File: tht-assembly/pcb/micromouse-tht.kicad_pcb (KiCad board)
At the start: 2 copper layers, 100 x 120 mm, 161 parts, among them J1 JST_XH_B2B-XH-A_1x02_P2.50mm_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, J10 AMASS_XT60-M_1x02_P7.20mm_Ver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, J11 PinSocket_1x08_P2.54mm_Vertic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, J12 PinSocket_1x08_P2.54mm_Vertic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, J13 PinSocket_1x22_P2.54mm_Vertic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, J14 PinSocket_1x22_P2.54mm_Vertic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, J15 PinSocket_1x06_P2.54mm_Vertic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, J5 JST_ZH_B6B-ZR_1x06_P1.50mm_Ve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, J6 JST_ZH_B6B-ZR_1x06_P1.50mm_Ve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, J8 PinHeader_1x06_P2.54mm_Vertic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, J9 JST_XH_B3B-XH-A_1x03_P2.50mm_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, Q1 TO-220-3_Vertical, Q121 TO-92_Inline, Q122 TO-92_Inline, Q123 TO-92_Inline, Q124 TO-92_Inline, Q125 TO-92_Inline, Q126 TO-92_Inline, Q131 TO-92_Inline, Q132 TO-92_Inline, Q133 TO-92_Inline, Q134 TO-92_Inline, Q135 TO-92_Inline, Q136 TO-92_Inline, Q137 TO-92_Inline, Q138 TO-92_Inline, Q16 TO-92_Inline, Q17 TO-92_Inline, Q18 TO-92_Inline, Q19 TO-92_Inline, Q2 LED_D5.0mm_IRBlack, Q3 LED_D5.0mm_IRBlack, Q34 TO-92_Inline, Q35 TO-92_Inline, Q4 LED_D5.0mm_IRBlack, Q5 LED_D5.0mm_IRBlack, Q6 LED_D5.0mm_IRBlack, Q7 LED_D5.0mm_IRBlack, SW1 SW_PUSH_6mm, SW2 SW_PUSH_6mm, SW3 SW_PUSH_6mm, SW4 SW_PUSH_6mm, SW5 SW_Slide_SPDT_Angled_CK_OS102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, SW6 SW_Slide_SPDT_Angled_CK_OS102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, U1 TO-220-5_Vertical, U4 DIP-24_W15.24mm, U7 TO-220-5_Vertical

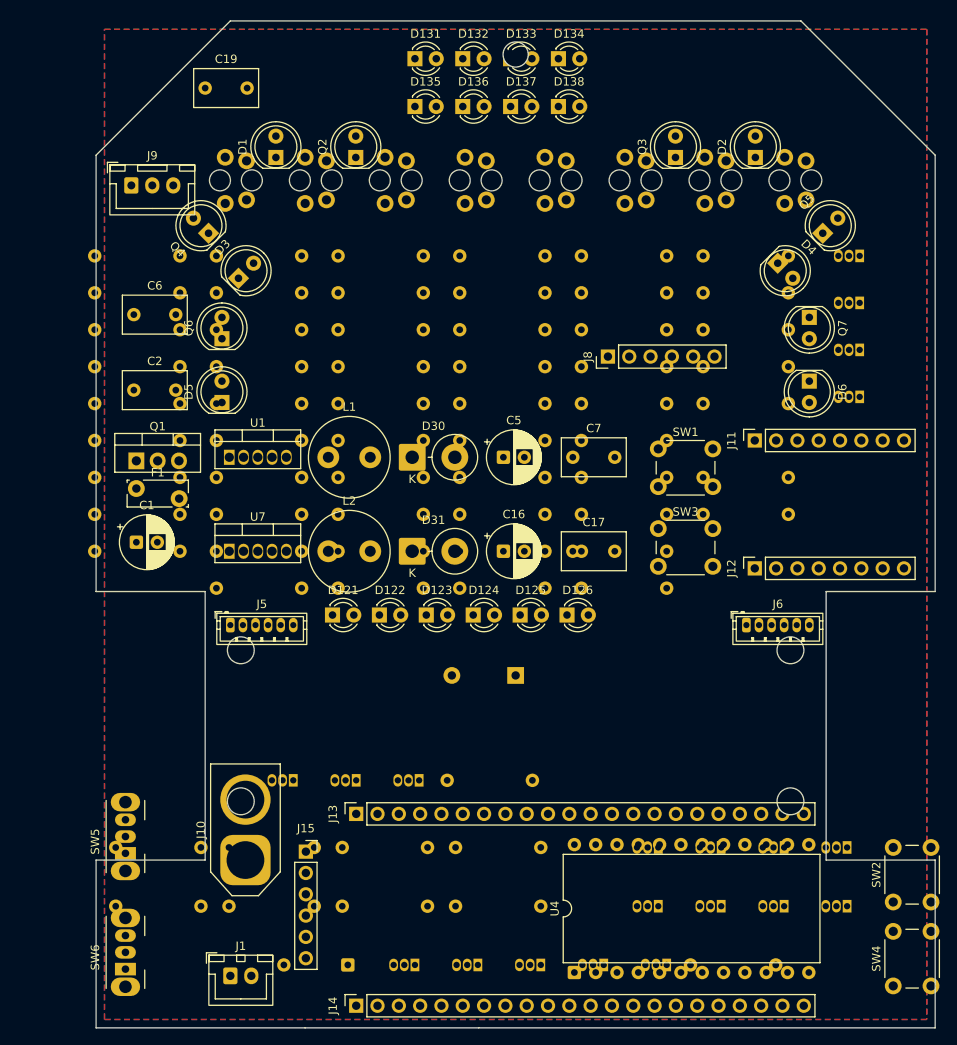
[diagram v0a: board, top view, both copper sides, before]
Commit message: THT M4 WIP: net-aware clustering placer + repair pass + visual floor-plan (11 overlaps, converging)
Replaces the routing-hostile bottom-grid placement (47% route-fail) with a
net-aware auto-placer: fixed anchors for geometry/edge parts, every support
part spiral-placed adjacent to its neighbours on the bottom face, then a
repair pass driving check_overlaps down using the accurate per-piece checker.
Down to 11 courtyard overlaps (from 83); remaining = buttons-vs-driver-socket
+ close optic pairs + mount-hole adjacencies. Router v3 (fast-fail, bounded,
incremental-save, logged) proven on the signal nets; spanning power/emitter
buses queued for hand-routing. WIP checkpoint -- not yet DRC-clean.

Co-Authored-By: Claude Fable 5 <noreply@anthropic.com>
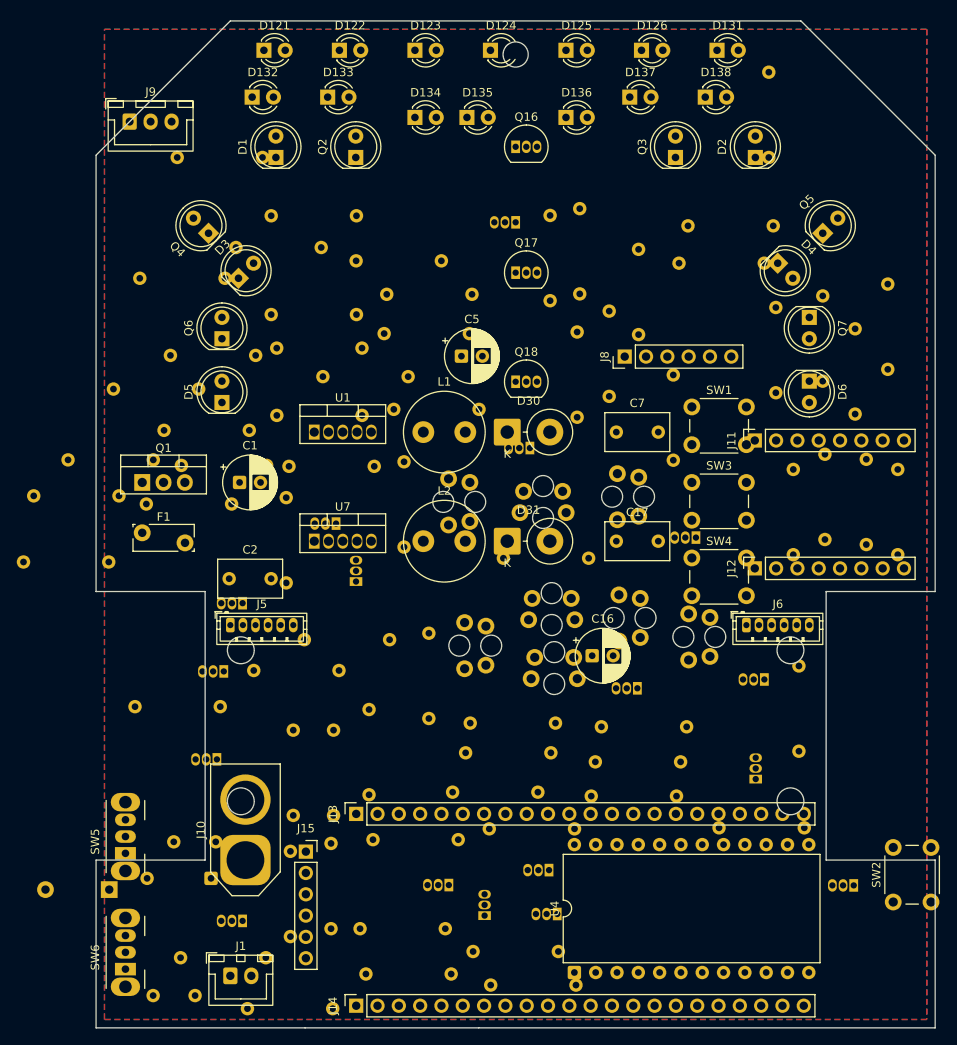
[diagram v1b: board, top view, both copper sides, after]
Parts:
- C19, C6: moved to B.Cu
- Q16, Q17, Q18: moved to F.Cu
- moved C19 108.2 mm to (11.8, 116.2), turned to 180 degrees
- moved Q16 93.8 mm to (50.0, 15.0), turned to 0 degrees
- moved R114 90.6 mm to (42.3, 113.6)
- moved R115 89.2 mm to (83.8, 87.0), turned to 90 degrees
- moved R101 84.0 mm to (86.9, 61.8), turned to 90 degrees
- moved R112 82.6 mm to (57.2, 114.9)
- moved Q17 82.0 mm to (50.0, 30.0), turned to 0 degrees
- moved R113 80.2 mm to (41.6, 108.2)
- moved R111 80.1 mm to (55.1, 110.9)
- moved R1 79.8 mm to (2.73, 56.6)
- moved R108 77.6 mm to (95.5, 63.6), turned to 90 degrees
- moved R102 75.6 mm to (91.8, 62.4), turned to 90 degrees
- moved R117 74.0 mm to (23.2, 109.1), turned to 90 degrees
- moved Q18 73.9 mm to (50.0, 43.0), turned to 0 degrees
- moved Q137 72.6 mm to (17.5, 107.2)
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
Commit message: THT placement: 5 courtyard overlaps (4 body-clear optic pairs + DevKit/bracket-hole mechanical conflict)
J6 relocated clear of the TB6612 socket; buttons to the open lower-centre;
nose LEDs dodge the castor hole. Remaining: the diagonal emitter/detector
clusters (body-clear, cosmetic) and -- the real finding -- the DevKitC-1
1x22 socket (56mm) overlaps a UKMARS motor-bracket mounting hole. The
100x120 SMD footprint cannot cleanly host a DevKit-based THT build + the
fixed bracket holes; needs a larger board or a different module mount.

Co-Authored-By: Claude Fable 5 <noreply@anthropic.com>
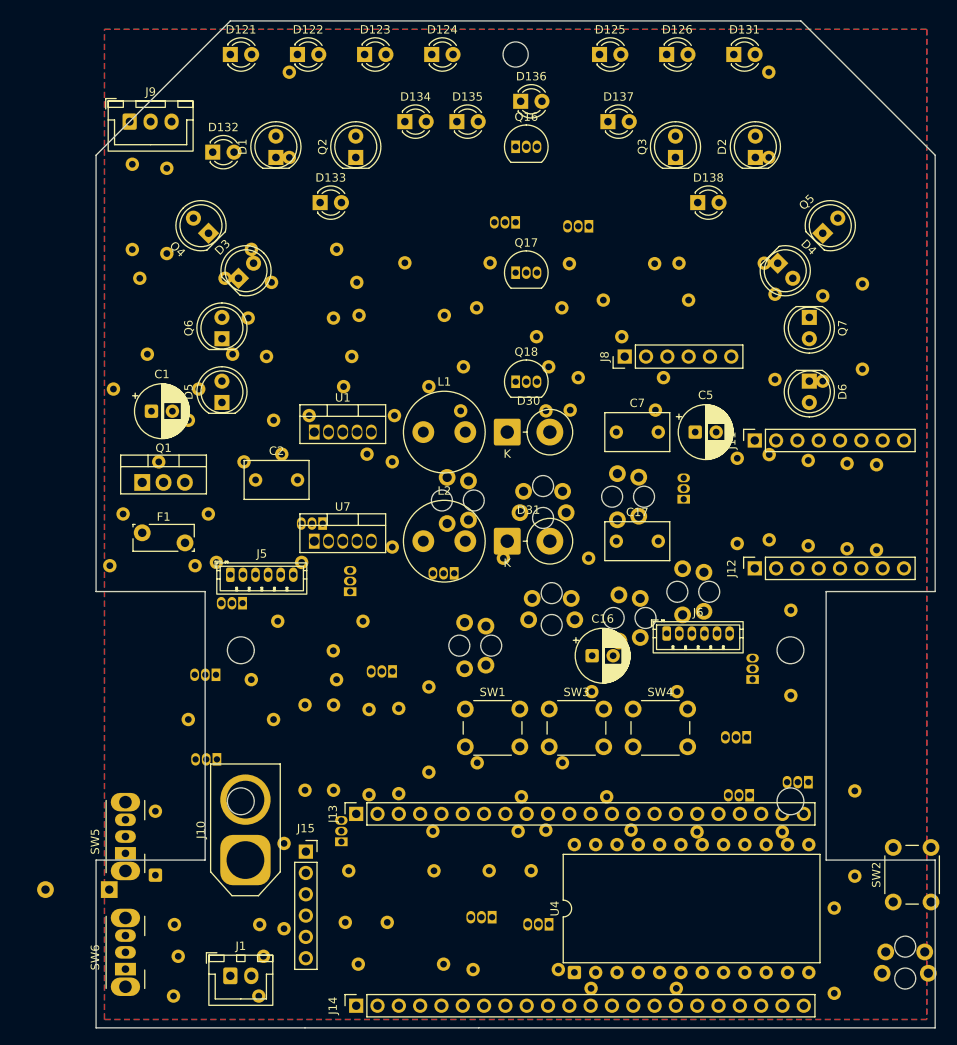
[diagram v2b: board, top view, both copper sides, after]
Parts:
- moved R107 86.9 mm to (93.0, 63.0), turned to 90 degrees
- moved R108 82.8 mm to (16.3, 39.7), turned to 180 degrees
- moved Q137 69.4 mm to (84.9, 90.7)
- moved R117 67.6 mm to (90.4, 101.9)
- moved Q138 60.4 mm to (42.7, 65.8)
- moved LS2 54.6 mm to (96.4, 112.2)
- moved R104 50.5 mm to (19.9, 111.5)
- moved R118 48.5 mm to (36.1, 92.1), turned to 90 degrees
- moved SW1 45.0 mm to (44.0, 82.0)
- moved C19 42.7 mm to (51.9, 101.3)
- moved R2 41.7 mm to (8.43, 27.7)
- moved R58 39.3 mm to (24.5, 64.5)
- moved Q124 39.2 mm to (58.7, 24.5)
- moved R105 38.1 mm to (91.3, 41.5)
- moved R142 36.4 mm to (28.7, 78.5)
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
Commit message: THT placement CLEAN: 0 courtyard overlaps (line array removed, 2 RGB LEDs added, JTAG dropped)
Per user: removed the line-follower array + mux (~50 parts -> board decongested
198->145 parts), added 2x ESP-driven common-cathode RGB LEDs (D40/D41,
Kingbright WP154A4, 6 LEDC channels via freed pins), dropped the redundant
external JTAG header (DevKit has USB-JTAG). DevKit socket recentred (x25.5) to
sit between the motor-bracket holes. Optic courtyards shrunk to body-true
circles (r=2.4) so the 45-deg diagonal emitter/detector pairs clear DRC.
verify_drc courtyard overlaps: 0. Next: route + DRC gate.

Co-Authored-By: Claude Fable 5 <noreply@anthropic.com>
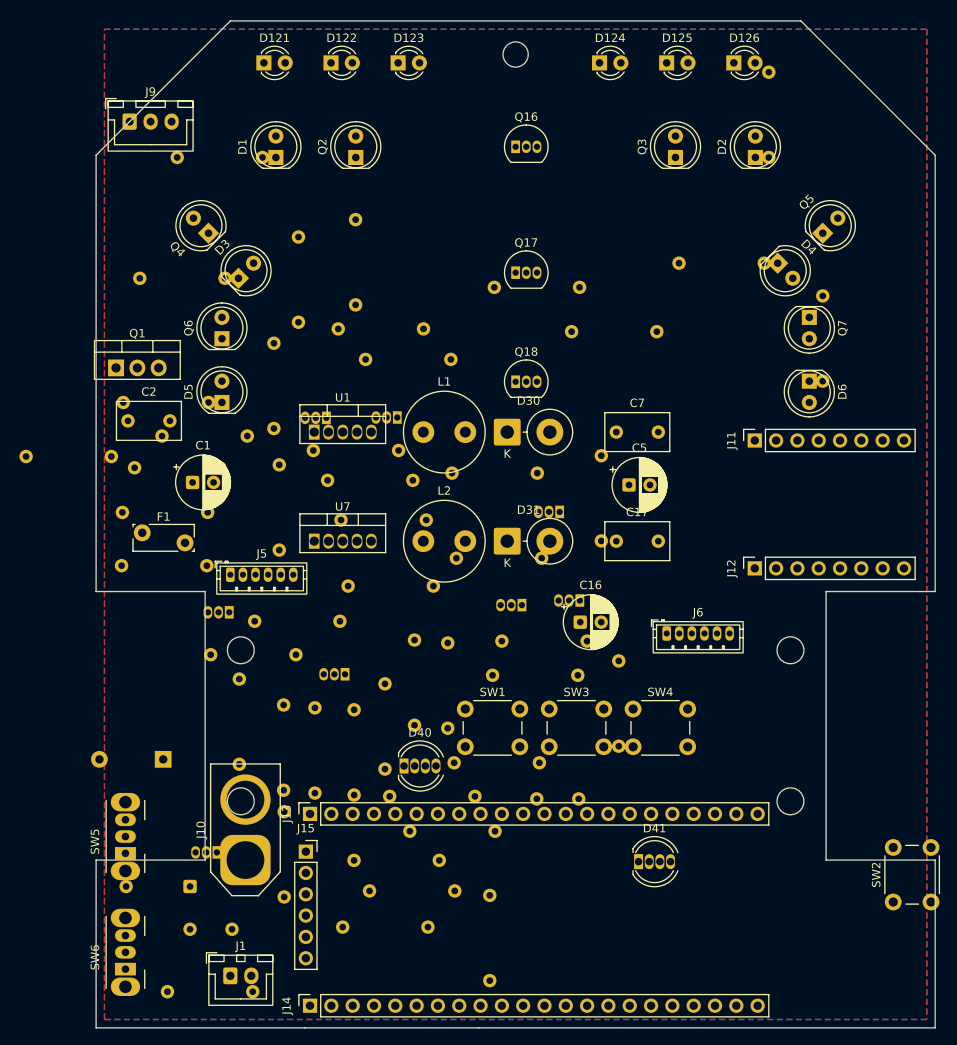
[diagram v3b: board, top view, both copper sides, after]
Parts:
- removed D131, D132, D133, D134, D135, D136, D137, D138: LED_D3.0mm, LED_D3.0mm
- removed J8: PinHeader_1x06_P2.54mm_Vertical, PinHeader_1x06_P2.54mm_Vertical
- removed LS1, LS2, LS3, LS4, LS5, LS6, LS7, LS8: TCRT5000, TCRT5000
- removed Q131, Q132, Q133, Q134, Q135, Q136, Q137, Q138, Q19: TO-92_Inline, TO-92_Inline
- removed R101, R102, R103, R104, R105, R106, R107, R108, R111, R112, R113, R114, R115, R116, R117, R118, R161, R162, R163, R164, R165, R166, R167, R168, R61: R_Axial_DIN0207_L6.3mm_D2.5mm_P10.16mm_Horizontal, R_Axial_DIN0207_L6.3mm_D2.5mm_P10.16mm_Horizontal
- removed U4: DIP-24_W15.24mm, DIP-24_W15.24mm
- added D40: LED_D5.0mm-4_RGB, LED_D5.0mm-4_RGB, F.Cu at (36.7, 88.8)
- added D41: LED_D5.0mm-4_RGB, LED_D5.0mm-4_RGB, F.Cu at (64.7, 100.2)
- added R201: R_Axial_DIN0207_L6.3mm_D2.5mm_P10.16mm_Horizontal, R_Axial_DIN0207_L6.3mm_D2.5mm_P10.16mm_Horizontal, B.Cu at (40.9, 100.0)
- added R202: R_Axial_DIN0207_L6.3mm_D2.5mm_P10.16mm_Horizontal, R_Axial_DIN0207_L6.3mm_D2.5mm_P10.16mm_Horizontal, B.Cu at (34.4, 89.2)
- added R203: R_Axial_DIN0207_L6.3mm_D2.5mm_P10.16mm_Horizontal, R_Axial_DIN0207_L6.3mm_D2.5mm_P10.16mm_Horizontal, B.Cu at (30.8, 92.2)
- added R204: R_Axial_DIN0207_L6.3mm_D2.5mm_P10.16mm_Horizontal, R_Axial_DIN0207_L6.3mm_D2.5mm_P10.16mm_Horizontal, B.Cu at (38.0, 83.9)
- added R205: R_Axial_DIN0207_L6.3mm_D2.5mm_P10.16mm_Horizontal, R_Axial_DIN0207_L6.3mm_D2.5mm_P10.16mm_Horizontal, B.Cu at (41.9, 84.3)
- added R206: R_Axial_DIN0207_L6.3mm_D2.5mm_P10.16mm_Horizontal, R_Axial_DIN0207_L6.3mm_D2.5mm_P10.16mm_Horizontal, B.Cu at (42.8, 103.7)
- moved R76 59.2 mm to (21.2, 48.6), turned to 90 degrees
- moved R9 48.7 mm to (57.4, 78.0), turned to 180 degrees
- moved R2 37.8 mm to (21.8, 63.1)
- moved R58 34.7 mm to (45.1, 92.4)
- moved R64 34.4 mm to (60.2, 62.0)
- moved Q124 34.2 mm to (55.2, 58.5)
- moved R78 25.3 mm to (46.9, 114.4)
- moved R1 24.8 mm to (1.82, 51.9), turned to 180 degrees
- moved R75 22.6 mm to (14.8, 53.2), turned to 180 degrees
- moved Q121 21.5 mm to (35.9, 47.3), turned to 180 degrees
- moved R146 21.3 mm to (58.5, 73.9), turned to 180 degrees
- moved D124 20.0 mm to (60.0, 5.00)
- moved C6 18.5 mm to (16.2, 108.2)
- moved Q122 17.3 mm to (50.8, 69.6)
- moved Q126 17.3 mm to (57.6, 69.1), turned to 180 degrees
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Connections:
- J13 pad 12: MUX_S3 -> BAT_MID_SENSE
- J13 pad 17: MUX_S0 -> RGB1_R
- J13 pad 18: MUX_S1 -> RGB1_G
- J13 pad 19: MUX_S2 -> RGB1_B
- J13 pad 20: LINE_EMIT -> RGB2_R
- J13 pad 21: unconnected-(J13-Pin_21-Pad21) -> RGB2_G
- J13 pad 7: MUX_SENSE -> VBAT_SENSE
- J14 pad 6: JTAG_TMS -> RGB2_B
- J14 pad 7: JTAG_TDI -> unconnected-(J14-Pin_7-Pad7)
- J14 pad 8: JTAG_TDO -> unconnected-(J14-Pin_8-Pad8)
- J14 pad 9: JTAG_TCK -> unconnected-(J14-Pin_9-Pad9)
